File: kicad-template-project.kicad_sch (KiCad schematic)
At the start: 1 part

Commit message: feat: initial layout
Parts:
- removed C1: 1 uF, chenry-footprint-lib:C_0402, symbol 0-chenry-component-lib:C_0402_1U
- added H1, H2, H3: MountingHole_Pad, MountingHole:MountingHole_2.2mm_M2_DIN965_Pad, symbol Mechanical:MountingHole_Pad
- added J1: Conn_01x02_Pin, Connector_AMASS:AMASS_XT30PW-F_1x02_P2.50mm_Horizontal, symbol Connector:Conn_01x02_Pin
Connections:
- new net PH0/PH_OUT: H1.1
- new net PH1/PH_OUT: H2.1
- new net PH2/PH_OUT: H3.1
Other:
- added sheet CAN (sn65hvd230.kicad_sch)
- added sheet ETH (LAN8651.kicad_sch)
- added sheet FPGA (ice40up5k.kicad_sch)
- added sheet MAG (hall-encoder.kicad_sch)
- added sheet MCU (stm32g0b1.kicad_sch)
- added sheet PH0 (phase-driver.kicad_sch)
- added sheet PH1 (phase-driver.kicad_sch)
- added sheet PH2 (phase-driver.kicad_sch)

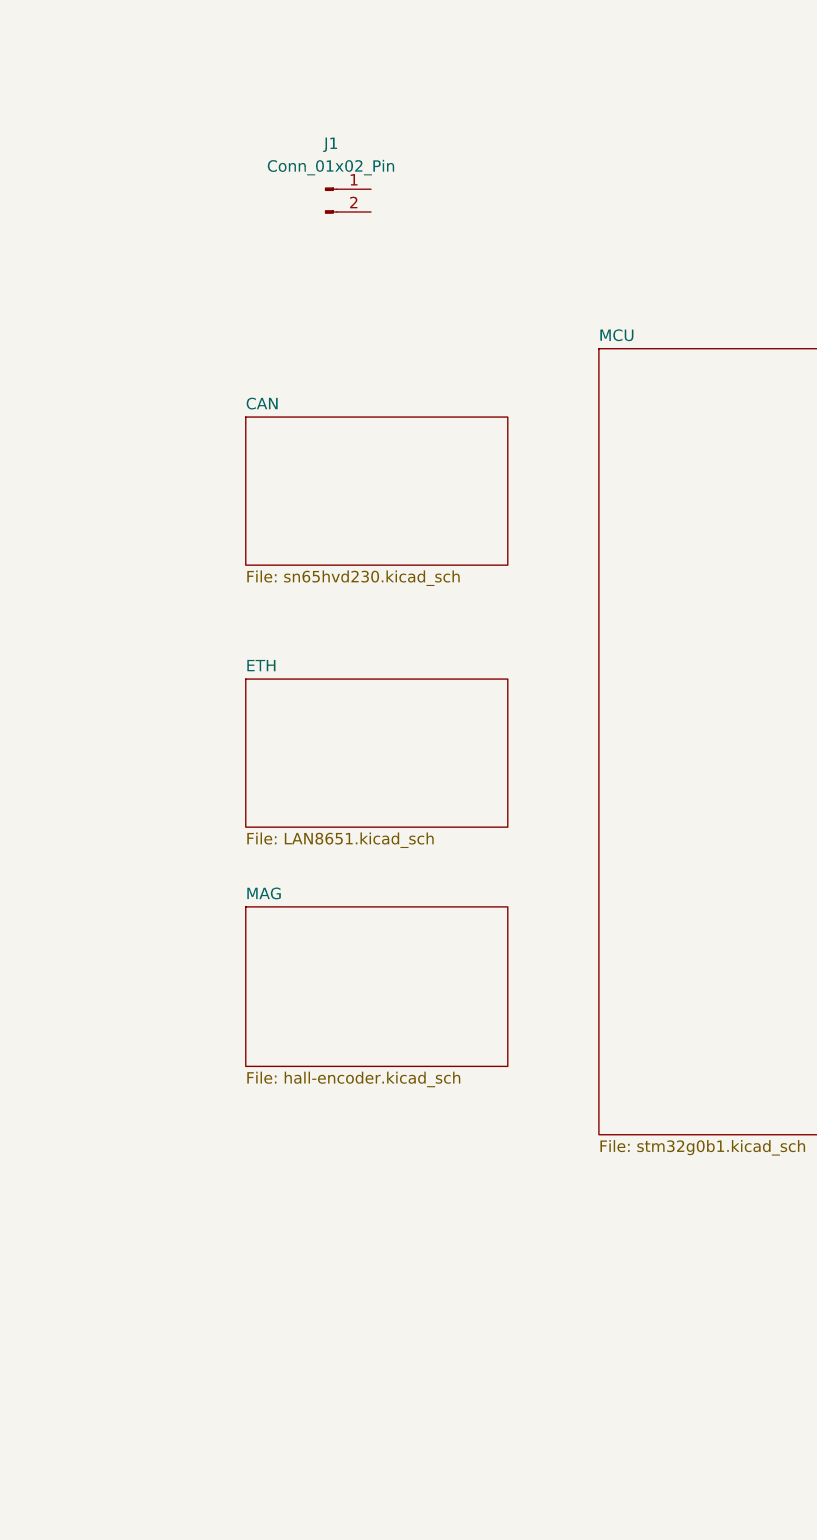
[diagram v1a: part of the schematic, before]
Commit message: fix: added switcher placeholders
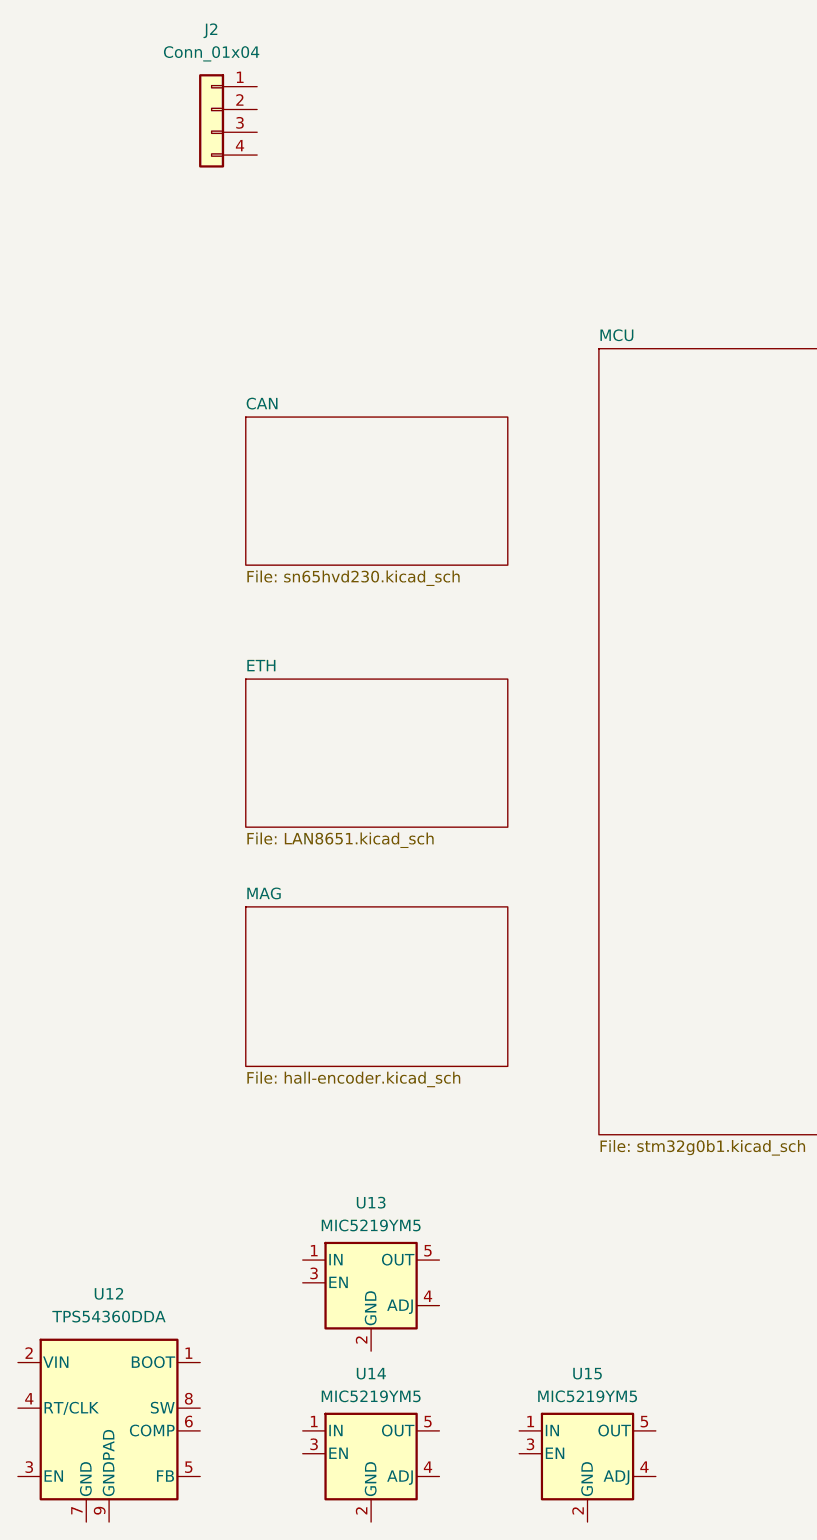
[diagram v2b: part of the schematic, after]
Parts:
- removed J1: Conn_01x02_Pin, Connector_AMASS:AMASS_XT30PW-F_1x02_P2.50mm_Horizontal, symbol Connector:Conn_01x02_Pin
- added J2: Conn_01x04, Connector_Molex:Molex_Micro-Fit_3.0_43045-0410_2x02-1MP_P3.00mm_Horizontal, symbol Connector_Generic:Conn_01x04
- added U12: TPS54360DDA, Package_SO:TI_SO-PowerPAD-8_ThermalVias, symbol Regulator_Switching:TPS54360DDA
- added U13, U14, U15: MIC5219YM5, Package_TO_SOT_SMD:SOT-23-5, symbol Regulator_Linear:MIC5219YM5

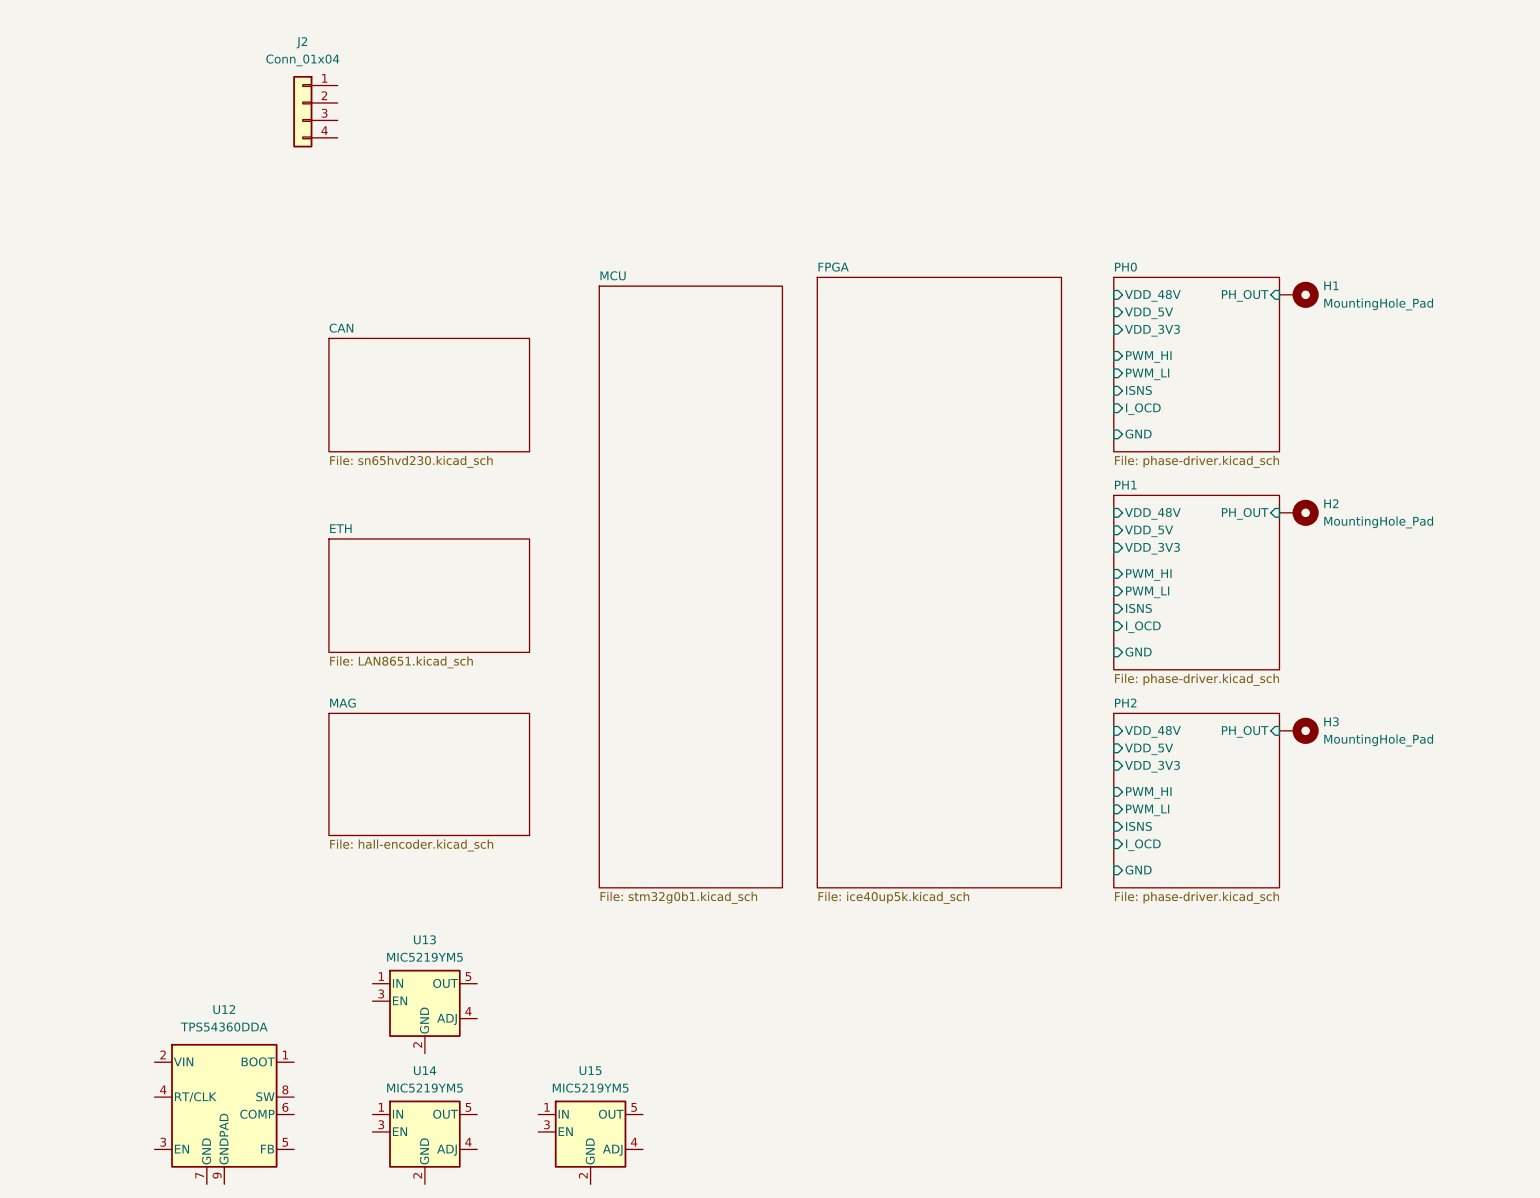
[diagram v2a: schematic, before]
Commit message: feat: done rough board placements for general shape
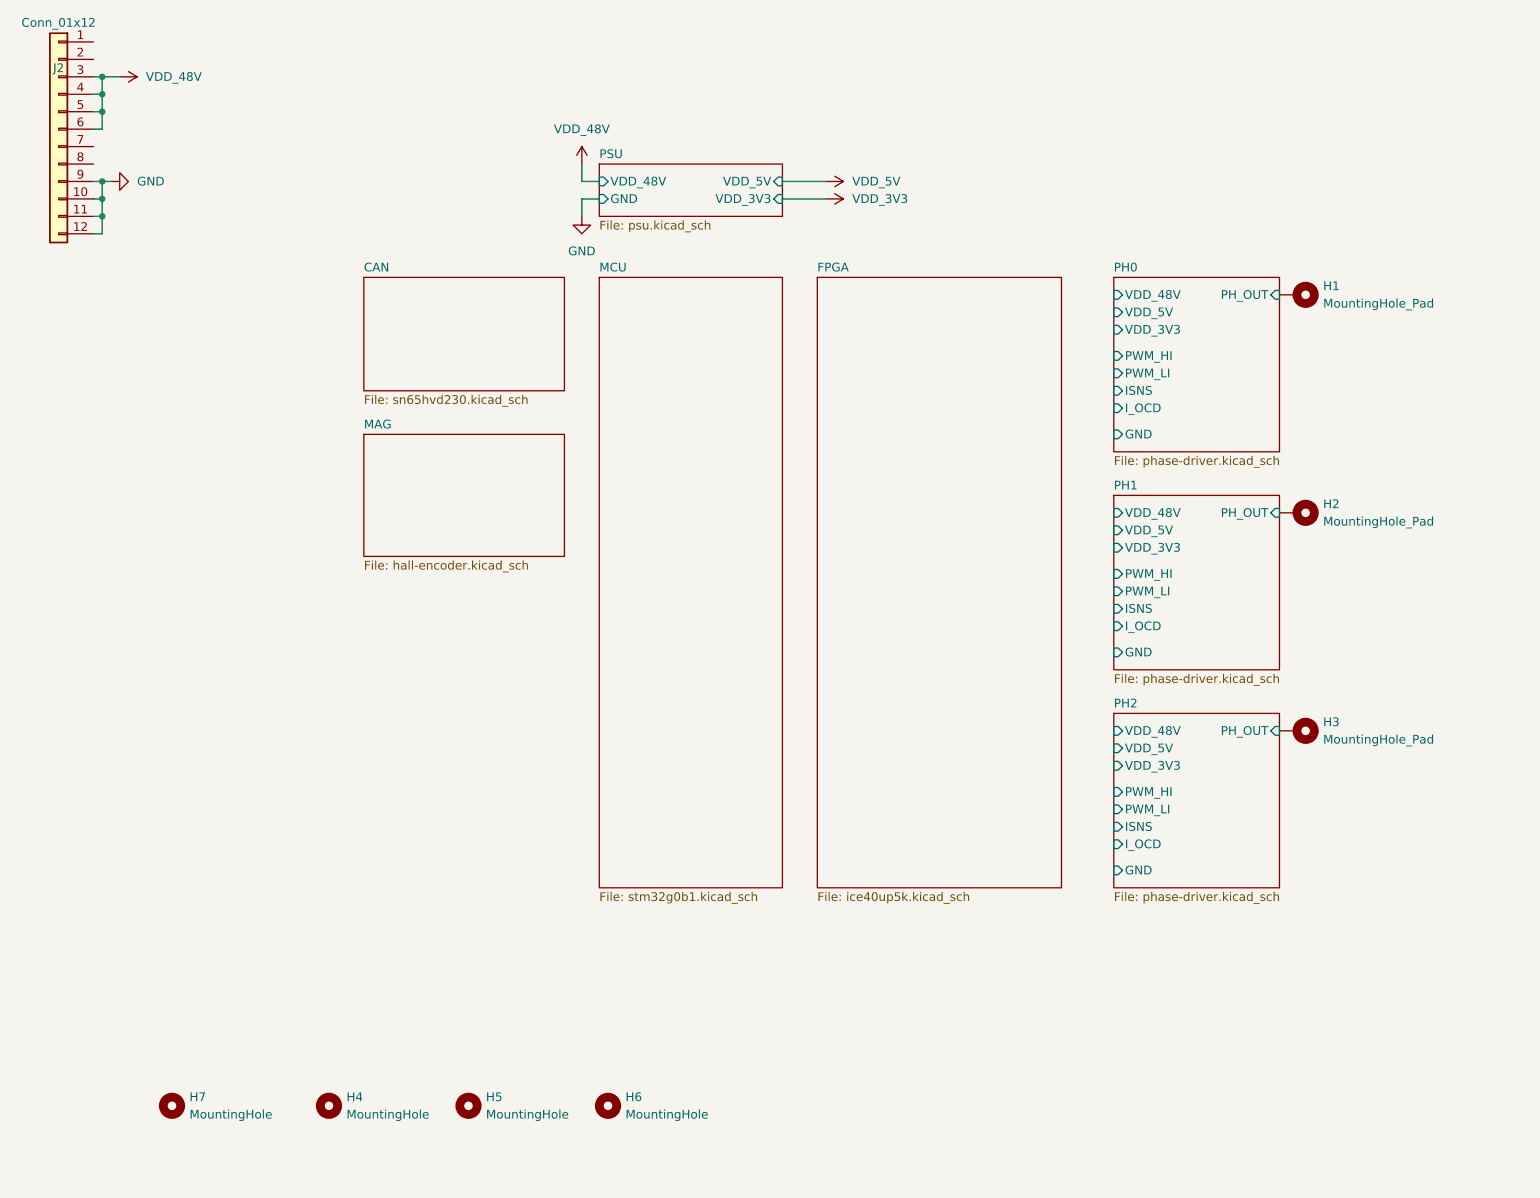
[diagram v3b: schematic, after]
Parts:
- removed U12: TPS54360DDA, Package_SO:TI_SO-PowerPAD-8_ThermalVias, symbol Regulator_Switching:TPS54360DDA
- removed U13, U14, U15: MIC5219YM5, Package_TO_SOT_SMD:SOT-23-5, symbol Regulator_Linear:MIC5219YM5
- added H4, H5, H6, H7: MountingHole, MountingHole:MountingHole_3.2mm_M3, symbol Mechanical:MountingHole
- J2: value Conn_01x04 -> Conn_01x12; footprint Connector_Molex:Molex_Micro-Fit_3.0_43045-0410_2x02-1MP_P3.00mm_Horizontal -> Connector_Molex:Molex_Micro-Fit_3.0_43045-1210_2x06-1MP_P3.00mm_Horizontal; symbol Connector_Generic:Conn_01x04 -> Connector_Generic:Conn_01x12
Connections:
- net VDD_48V: now reaches J2.3 (Pin_3)
- net VDD_48V: now also J2.4 (Pin_4), J2.5 (Pin_5), J2.6 (Pin_6)
- new net GND: J2.10 (Pin_10), J2.11 (Pin_11), J2.12 (Pin_12), J2.9 (Pin_9)
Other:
- removed sheet ETH
- added sheet PSU (psu.kicad_sch)

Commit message: fix: fleshignout schematic for mcu, fpga and mag + peripherals
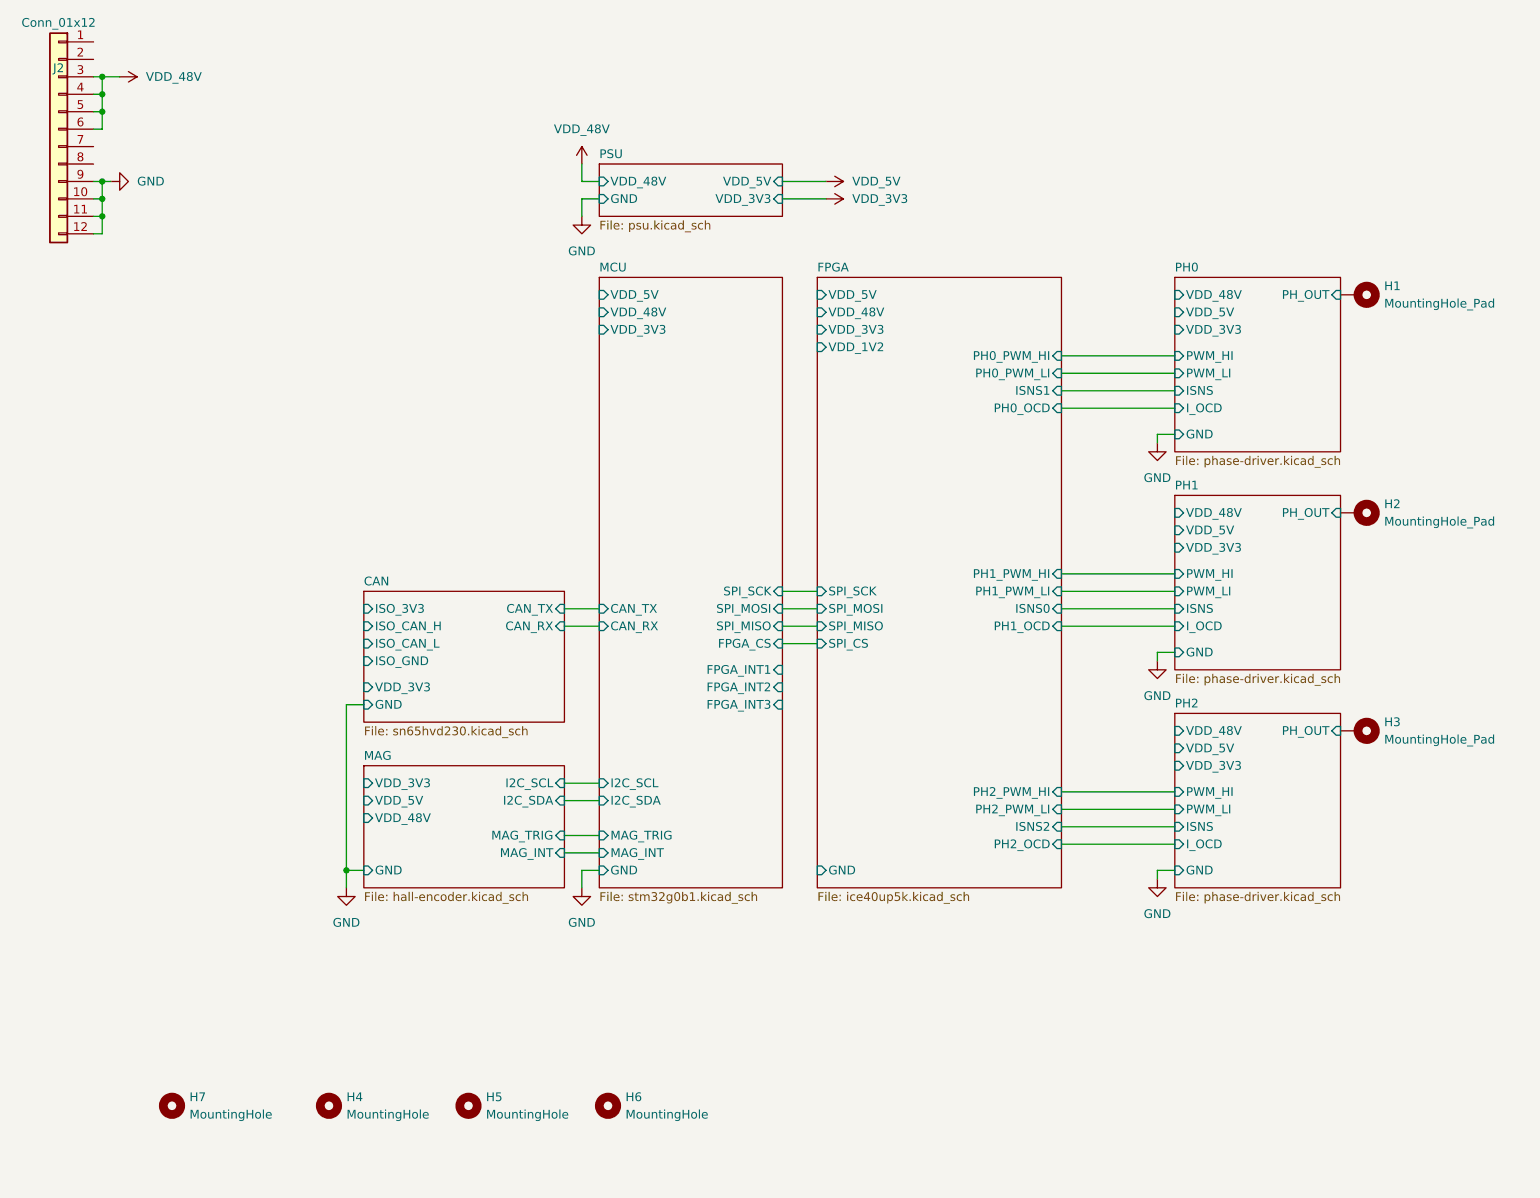
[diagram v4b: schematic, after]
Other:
- sheet CAN ports: added CAN_RX, CAN_TX, GND, ISO_3V3, ISO_CAN_H, ISO_CAN_L, ISO_GND, VDD_3V3; removed none
- sheet FPGA ports: added GND, ISNS0, ISNS1, ISNS2, PH0_OCD, PH0_PWM_HI, PH0_PWM_LI, PH1_OCD, PH1_PWM_HI, PH1_PWM_LI, PH2_OCD, PH2_PWM_HI, PH2_PWM_LI, SPI_CS, SPI_MISO, SPI_MOSI, SPI_SCK, VDD_1V2, VDD_3V3, VDD_48V, VDD_5V; removed none
- sheet MAG ports: added GND, I2C_SCL, I2C_SDA, MAG_INT, MAG_TRIG, VDD_3V3, VDD_48V, VDD_5V; removed none
- sheet MCU ports: added CAN_RX, CAN_TX, FPGA_CS, FPGA_INT1, FPGA_INT2, FPGA_INT3, GND, I2C_SCL, I2C_SDA, MAG_INT, MAG_TRIG, SPI_MISO, SPI_MOSI, SPI_SCK, VDD_3V3, VDD_48V, VDD_5V; removed none
- moved on the sheet: H1, H2, H3
